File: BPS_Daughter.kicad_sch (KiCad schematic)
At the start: 0 parts

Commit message: bps leader
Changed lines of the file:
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@@
 	(generator_version "9.0")
 	(paper "A4")
+	(hierarchical_label "Drive_ARR"
+		(shape output)
+		(at 121.92 130.81 0)
+		(effects
+			(font
+				(size 1.27 1.27)
+			)
+			(justify left)
+		)
+	)
 	(hierarchical_label "+Sens_HV-"
 		(shape output)
 		(at 121.92 95.25 0)
+		(effects
+			(font
+				(size 1.27 1.27)
+			)
+			(justify left)
+		)
+	)
+	(hierarchical_label "-Sens_ARR"
+		(shape output)
+		(at 121.92 135.255 0)
 		(effects
 			(font
@@
 		)
 	)
+	(hierarchical_label "+Sens_ARR"
+		(shape output)
+		(at 121.92 127 0)
+		(effects
+			(font
+				(size 1.27 1.27)
+			)
+			(justify left)
+		)
+	)
 	(hierarchical_label "GND_HV+"
 		(shape output)
 		(at 121.92 85.09 0)
+		(effects
+			(font
+				(size 1.27 1.27)
+			)
+			(justify left)
+		)
+	)
+	(hierarchical_label "Fan1"
+		(shape output)
+		(at 121.92 146.05 0)
 		(effects
 			(font
@@
 		(shape output)
 		(at 121.92 107.95 0)
+		(effects
+			(font
+				(size 1.27 1.27)
+			)
+			(justify left)
+		)
+	)
+	(hierarchical_label "GND_ARR"
+		(shape output)
+		(at 121.92 139.7 0)
 		(effects
 			(font
@@
 		(effects
 			(font
+				(size 1.27 1.27)
+			)
+			(justify left)
+		)
+	)
+	(hierarchical_label "Fan2"
+		(shape output)
+		(at 121.92 150.495 0)
+		(effects
+			(font

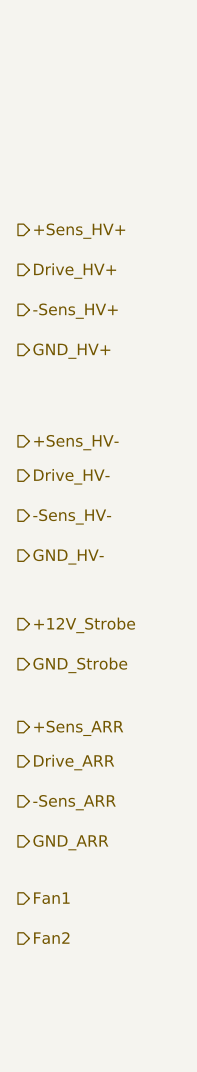
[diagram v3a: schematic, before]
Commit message: new precharge architecture
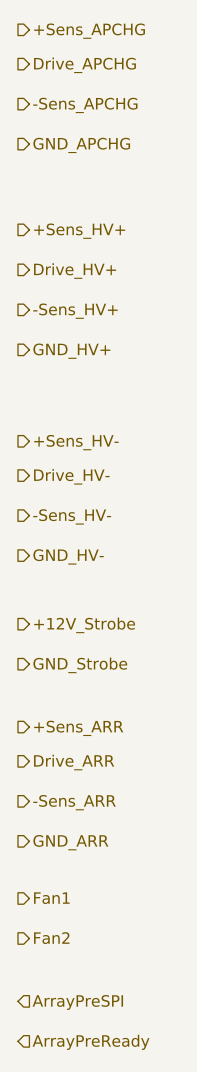
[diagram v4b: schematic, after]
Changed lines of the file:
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@@
 	(generator_version "9.0")
 	(paper "A4")
+	(hierarchical_label "+Sens_APCHG"
+		(shape output)
+		(at 121.92 49.53 0)
+		(effects
+			(font
+				(size 1.27 1.27)
+			)
+			(justify left)
+		)
+	)
 	(hierarchical_label "Drive_ARR"
 		(shape output)
@@
 		)
 	)
+	(hierarchical_label "ArrayPreReady"
+		(shape input)
+		(at 121.92 161.925 0)
+		(effects
+			(font
+				(size 1.27 1.27)
+			)
+			(justify left)
+		)
+	)
 	(hierarchical_label "GND_HV-"
 		(shape output)
@@
 		(effects
 			(font
+				(size 1.27 1.27)
+			)
+			(justify left)
+		)
+	)
+	(hierarchical_label "ArrayPreSPI"
+		(shape input)
+		(at 121.92 157.48 0)
+		(effects
+			(font
+				(size 1.27 1.27)
+			)
+			(justify left)
+		)
+	)
+	(hierarchical_label "-Sens_APCHG"
+		(shape output)
+		(at 121.92 57.785 0)
+		(effects
+			(font
+				(size 1.27 1.27)
+			)
+			(justify left)
+		)
+	)
+	(hierarchical_label "Drive_APCHG"
+		(shape output)
+		(at 121.92 53.34 0)
+		(effects
+			(font
+				(size 1.27 1.27)
+			)
+			(justify left)
+		)
+	)
+	(hierarchical_label "GND_APCHG"
+		(shape output)
+		(at 121.92 62.23 0)
+		(effects
+			(font
